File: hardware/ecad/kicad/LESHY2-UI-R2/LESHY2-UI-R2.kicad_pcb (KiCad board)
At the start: 6 copper layers, 80 x 150 mm, 432 parts, among them J1 Hirose FH34SRJ-50S-0.5SH(50), J10 Samtec FTSH-105-01-L-DV-K-P-TR, J11 GCT USB4105-GF-A, J12 GCT RFPC-SMA31-FN-175-A, J13 Hirose U.FL-R-SMT-1(80), J14 GCT RFPC-SMA31-FN-175-A, J15 Hirose U.FL-R-SMT-1(80), J16 GCT RFPC-SMA31-FN-175-A, J17 Hirose U.FL-R-SMT-1(80), J18 Hirose FX8C-80P-SV1(92), J2 Samtec FTSH-105-01-L-DV-K-P-TR, J3 GCT RFPC-SMA32-FN-175-A, J4 Hirose U.FL-R-SMT-1(80), J5 Hirose DM3AT-SF-PEJM5, J6 Samtec FTSH-105-01-L-DV-K-P-TR, J7 GCT RFPC-SMA32-FN-175-A, J8 Hirose U.FL-R-SMT-1(80), J9 GCT USB4105-GF-A, Q1 Diodes Incorporated DMN2056U-7, Q2 Diodes Incorporated 2N7002DW-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, Q3 Diodes Incorporated DMN2056U-7, Q4 Diodes Incorporated DMN2056U-7, Q5 Diodes Incorporated DMN2056U-7, Q6 Diodes Incorporated 2N7002DW-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, SW1 Alps Alpine SKRTLAE010, SW10 OMRON B3S-1100P, SW11 OMRON B3S-1100P, SW12 OMRON B3S-1100P, SW13 OMRON B3S-1100P, SW14 OMRON B3S-1100P, SW15 OMRON B3S-1100P, SW16 OMRON B3S-1100P, SW17 OMRON B3S-1100P, SW18 Alps Alpine SKRTLAE010, SW19 Alps Alpine SKRTLAE010, SW2 Alps Alpine SKRTLAE010, SW20 Alps Alpine SKRTLAE010, SW21 Alps Alpine SKRTLAE010, SW3 OMRON B3S-1100P, SW4 OMRON B3S-1100P, SW5 OMRON B3S-1100P, SW6 OMRON B3S-1100P, SW7 OMRON B3S-1100P, SW8 OMRON B3S-1100P, SW9 OMRON B3S-1100P, U1 ESP32-S3-WROOM-1U-N16R8, U10 Texas Instruments TPS22919DCKR, U11 SN74LVC1G07DCKR, U12 Texas Instruments TPD8E003DQDR, U13 TCA9539PWR, U14 ESP32-C5-WROOM-1U-N8R8, U15 Texas Instruments TPD4E05U06D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, U16 KYOCERA AVX CP0603Q5425ENTR, U17 74LVC2G14GV,125, U18 SN74LVC1G74DCUR, U19 74HC20PW,118, U2 Texas Instruments TPD4E05U06D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, U20 74LVC2G14GV,125, U21 Texas Instruments TPD2EUSB30A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, U22 onsemi FSUSB42MUX, U23 Vishay TSMP95000TT, U24 Vishay TSOP75238TR, U25 Texas Instruments TPS22919DCKR, U26 Nexperia 74LVC2G126DP,125, U27 SN74LVC1G08DCKR, U28 SC1512-A4, U29 Texas Instruments TPD4E05U06D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, U3 KYOCERA AVX CP0603Q5425ENTR, U30 Texas Instruments TPD2EUSB30A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, U31 onsemi FSUSB42MUX, U32 Analog Devices AD8314ARMZ-REEL, U33 Analog Devices AD8314ARMZ-REEL, U34 Analog Devices AD8314ARMZ-REEL, U35 Ebyte E01-ML01SP4, U36 TTM Technologies DC2337J5010A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, U37 Nexperia 74LVC126APW,118, U38 Nexperia 74LVC2G126DP,125, U39 Ebyte E01-ML01SP4, U4 Texas Instruments TPS2553DRVR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, U40 TTM Technologies DC2337J5010A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

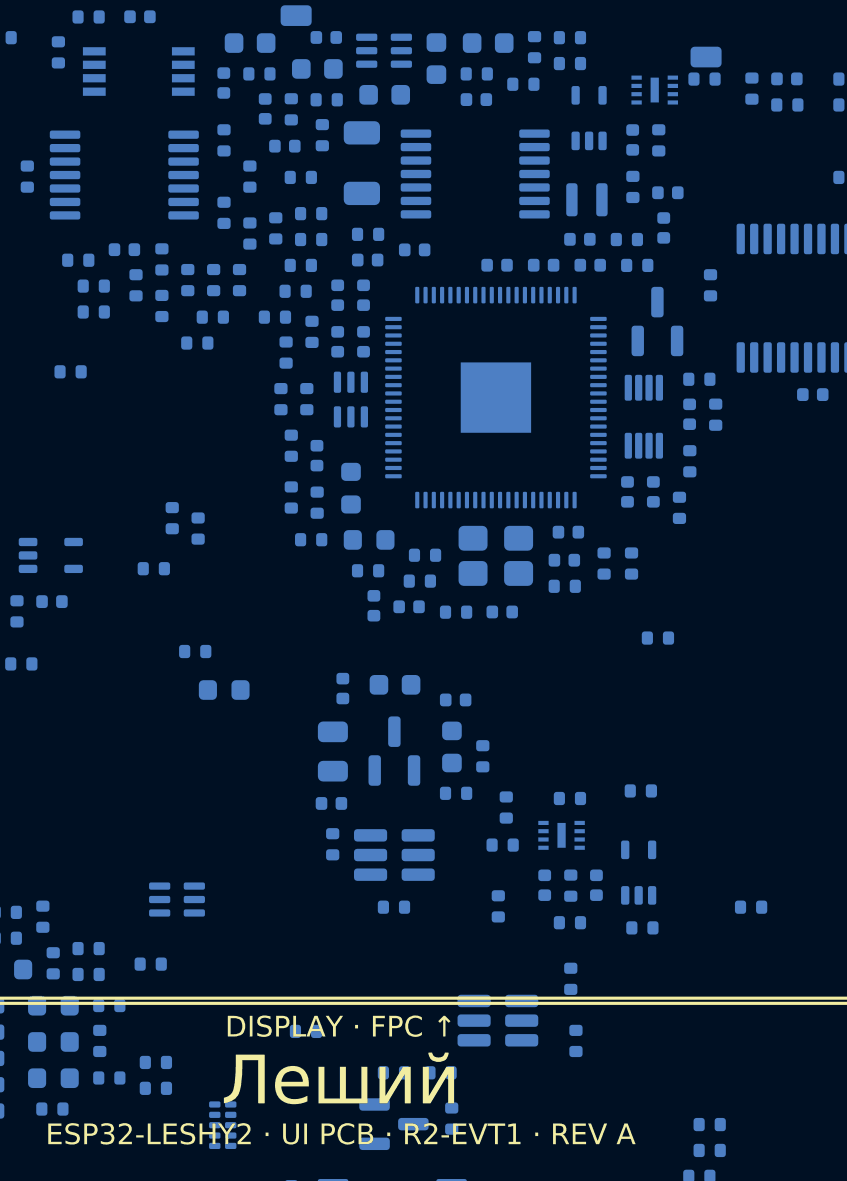
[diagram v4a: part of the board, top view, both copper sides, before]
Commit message: Audit critical placement by pad distance
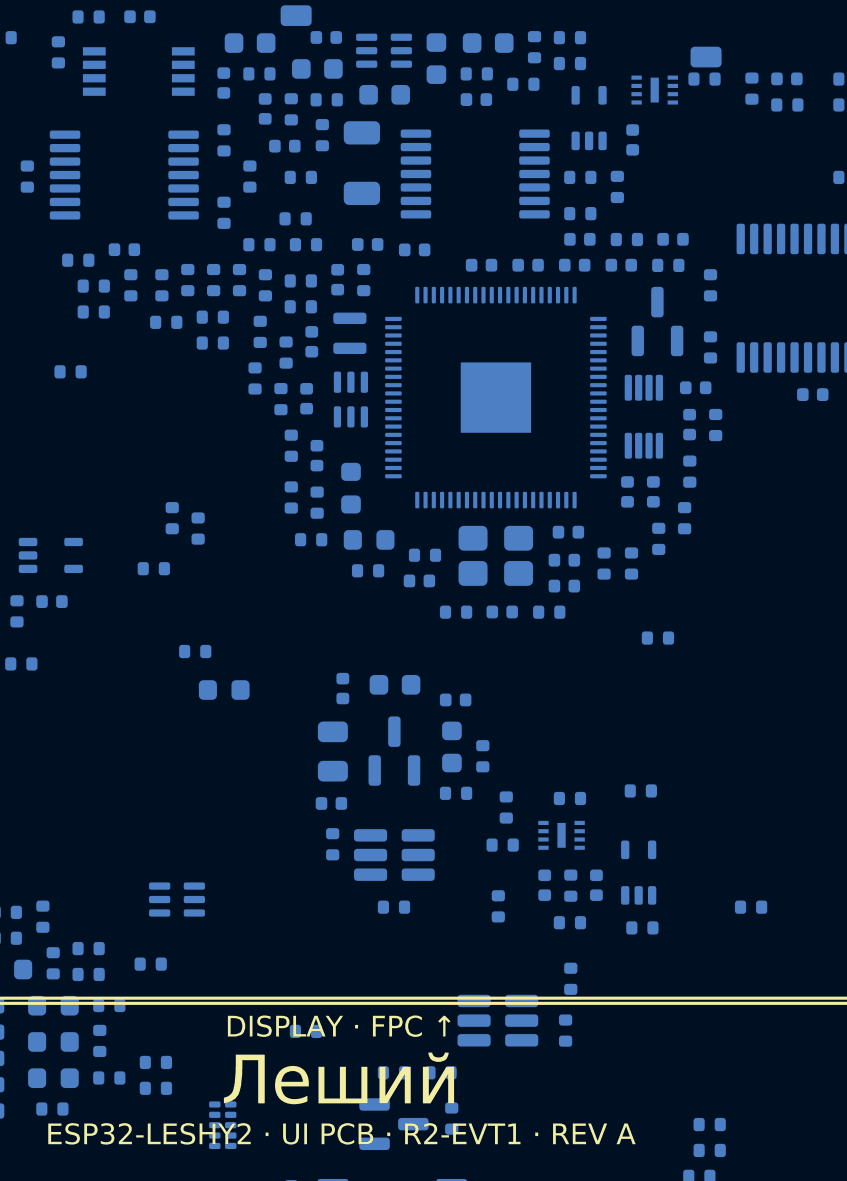
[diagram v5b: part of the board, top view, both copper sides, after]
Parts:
- moved R173 20.5 mm to (57.9, 72.6)
- moved C58 18.1 mm to (49.1, 68.6), turned to 0 degrees
- moved C56 17.6 mm to (41.3, 67.6)
- moved R192 16.5 mm to (50.1, 85.4), turned to 0 degrees
- moved C46 16.1 mm to (38.9, 77.8), turned to 90 degrees
- moved C52 15.7 mm to (43.8, 83.9)
- moved R145 14.8 mm to (41.1, 69.3), turned to 90 degrees
- moved C42 14.3 mm to (50.8, 82.9)
- moved C53 13.5 mm to (50.8, 84.1), turned to 0 degrees
- moved L1 13.1 mm to (40.4, 71.9), turned to 90 degrees
- moved C43 13.0 mm to (53.6, 68.6), turned to 0 degrees
- moved C41 12.6 mm to (53.9, 79.6), turned to 90 degrees
- moved C55 12.0 mm to (51.6, 67.4), turned to 0 degrees
- moved C50 11.9 mm to (39.9, 69.3), turned to 90 degrees
- moved R172 11.7 mm to (55.8, 68.6), turned to 0 degrees
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
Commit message: Start reviewed H6 manual copper
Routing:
- net /UI_30_HUB_RP_CORE_SERVICE/HUB_RP_VREG_LX_SW: track 0.00 -> 4.62 mm

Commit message: Route RP2354 crystal networks
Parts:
- moved R131 0.67 mm to (43.8, 82.0), turned to 90 degrees
- turned Y1 to 180 degrees
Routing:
- net /UI_30_HUB_RP_CORE_SERVICE/HUB_RP_XOUT_CRYSTAL: track 0.00 -> 9.49 mm
- net /UI_30_HUB_RP_CORE_SERVICE/HUB_RP_XIN: track 0.00 -> 7.61 mm
- net /UI_30_HUB_RP_CORE_SERVICE/HUB_RP_XOUT: track 0.00 -> 4.46 mm
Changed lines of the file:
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@@
 	(footprint "Crystal:Crystal_SMD_Abracon_ABM8G-4Pin_3.2x2.5mm"
 		(layer "B.Cu")
-		(at 47.495 82.645)
+		(at 47.495 82.645 180)
 		(descr "Abracon ABM8G, Miniature Ceramic Crystal, 3.2x2.5mm package, SMD, http://www.abracon.com/Resonators/ABM8G.pdf")
 		(property "Reference" "Y1"
-			(at 0 2.45 180)
+			(at 0 2.45 0)
 			(layer "B.SilkS")
 			(hide yes)
@@
 		)
 		(property "Value" "Abracon ABM8-272-T3"
-			(at 0 -2.45 180)
+			(at 0 -2.45 0)
 			(layer "B.Fab")
 			(hide yes)
@@
 		)
 		(property "Datasheet" ""
-			(at 0 0 180)
+			(at 0 0 0)
 			(layer "B.Fab")
 			(hide yes)
@@
 		)
 		(property "Description" "abracon_abm8_272_t3"
-			(at 0 0 180)
+			(at 0 0 0)
 			(layer "B.Fab")
 			(hide yes)
@@
 		)
 		(property "KiLib_Generator" "crystal_resonator_oscillator"
-			(at 0 0 180)
+			(at 0 0 0)
 			(layer "B.SilkS")
 			(hide yes)
@@
 		)
 		(property "Leshy2Instance" "hub_rp_clock"
-			(at 0 0 180)
+			(at 0 0 0)
 			(layer "B.SilkS")
 			(hide yes)
@@
 		(duplicate_pad_numbers_are_jumpers no)
 		(fp_line
-			(start -2.06 -1.71)
-			(end 2.06 -1.71)
+			(start -2.06 1.71)
+			(end -2.06 -1.71)
 			(stroke
 				(width 0.12)
@@
 		)
 		(fp_line
-			(start -2.06 1.71)
-			(end -2.06 -1.71)
+			(start -2.06 -1.71)
+			(end 2.06 -1.71)
 			(stroke
 				(width 0.12)
@@
 		)
 		(fp_text user "${REFERENCE}"
-			(at 0 0 180)
+			(at 0 0 0)
 			(layer "B.Fab")
 			(effects
@@
 		)
 		(pad "1" smd roundrect
-			(at -1.1 -0.85)
+			(at -1.1 -0.85 180)
 			(size 1.4 1.2)
 			(layers "B.Cu" "B.Mask" "B.Paste")
@@
 		)
 		(pad "2" smd roundrect
-			(at 1.1 -0.85)
+			(at 1.1 -0.85 180)
 			(size 1.4 1.2)
 			(layers "B.Cu" "B.Mask" "B.Paste")
@@
 		)
 		(pad "3" smd roundrect
-			(at 1.1 0.85)
+			(at 1.1 0.85 180)
 			(size 1.4 1.2)
 			(layers "B.Cu" "B.Mask" "B.Paste")
@@
 		)
 		(pad "4" smd roundrect
-			(at -1.1 0.85)
+			(at -1.1 0.85 180)
 			(size 1.4 1.2)
 			(layers "B.Cu" "B.Mask" "B.Paste")
@@
 	(footprint "Resistor_SMD:R_0402_1005Metric"
 		(layer "B.Cu")
-		(at 44.075 82.615 180)
+		(at 43.8 82 90)
 		(descr "Resistor SMD 0402 (1005 Metric), square (rectangular) end terminal, IPC-7351 nominal, (Body size source: IPC-SM-782 page 72, https://www.pcb-3d.com/wordpress/wp-content/uploads/ipc-sm-782a_amendment_1_and_2.pdf)")
 		(tags "resistor")
 		(property "Reference" "R131"
-			(at 0 1.17 0)
+			(at 0 1.17 270)
 			(layer "B.SilkS")
 			(hide yes)
@@
 		)
 		(property "Value" "Yageo RC0402FR-071KL"
-			(at 0 -1.17 0)
+			(at 0 -1.17 270)
 			(layer "B.Fab")
 			(hide yes)
@@
 		)
 		(property "Datasheet" ""
-			(at 0 0 0)
+			(at 0 0 270)
 			(layer "B.Fab")
 			(hide yes)
@@
 		)
 		(property "Description" "yageo_rc0402fr_071kl"
-			(at 0 0 0)
+			(at 0 0 270)
 			(layer "B.Fab")
 			(hide yes)
@@
 		)
 		(property "KiLib_Generator" "SMD_2terminal_chip_molded"
-			(at 0 0 0)
+			(at 0 0 270)
 			(layer "B.SilkS")
 			(hide yes)
@@
 		)
 		(property "Leshy2Instance" "hub_rp_clock_series"
-			(at 0 0 0)
+			(at 0 0 270)
 			(layer "B.SilkS")
 			(hide yes)
@@
 		(duplicate_pad_numbers_are_jumpers no)
 		(fp_line
-			(start -0.153641 0.38)
-			(end 0.153641 0.38)
+			(start -0.153641 -0.38)
+			(end 0.153641 -0.38)
 			(stroke
 				(width 0.12)
@@
 		)
 		(fp_line
-			(start -0.153641 -0.38)
-			(end 0.153641 -0.38)
+			(start -0.153641 0.38)
+			(end 0.153641 0.38)
 			(stroke
 				(width 0.12)
@@
 		)
 		(fp_text user "${REFERENCE}"
-			(at 0 0 0)
+			(at 0 0 270)
 			(layer "B.Fab")
 			(effects
@@
 		)
 		(pad "1" smd roundrect
-			(at -0.51 0 180)
+			(at -0.51 0 90)
 			(size 0.54 0.64)
 			(layers "B.Cu" "B.Mask" "B.Paste")
@@
 		)
 		(pad "2" smd roundrect
-			(at 0.51 0 180)
+			(at 0.51 0 90)
 			(size 0.54 0.64)
 			(layers "B.Cu" "B.Mask" "B.Paste")
@@
 	)
 	(segment
+		(start 49.55 80.7)
+		(end 50.52 81.5)
+		(width 0.15)
+		(layer "B.Cu")
+		(net "/UI_30_HUB_RP_CORE_SERVICE/HUB_RP_XIN")
+	)
+	(segment
+		(start 47.7 80.7)
+		(end 49.55 80.7)
+		(width 0.15)
+		(layer "B.Cu")
+		(net "/UI_30_HUB_RP_CORE_SERVICE/HUB_RP_XIN")
+	)
+	(segment
+		(start 47.7 79.95)
+		(end 47.7 80.7)
+		(width 0.15)
+		(layer "B.Cu")
+		(net "/UI_30_HUB_RP_CORE_SERVICE/HUB_RP_XIN")
+	)
+	(segment
+		(start 49.55 80.7)
+		(end 49.55 83.5)
+		(width 0.15)
+		(layer "B.Cu")
+		(net "/UI_30_HUB_RP_CORE_SERVICE/HUB_RP_XIN")
+	)
+	(segment
+		(start 49.55 83.5)
+		(end 48.595 83.495)
+		(width 0.15)
+		(layer "B.Cu")
+		(net "/UI_30_HUB_RP_CORE_SERVICE/HUB_RP_XIN")
+	)
+	(segment
+		(start 45 80.65)
+		(end 43.8 81.49)
+		(width 0.15)
+		(layer "B.Cu")
+		(net "/UI_30_HUB_RP_CORE_SERVICE/HUB_RP_XOUT")
+	)
+	(segment
+		(start 47.3 80.65)
+		(end 45 80.65)
+		(width 0.15)
+		(layer "B.Cu")
+		(net "/UI_30_HUB_RP_CORE_SERVICE/HUB_RP_XOUT")
+	)
+	(segment
+		(start 47.3 79.95)
+		(end 47.3 80.65)
+		(width 0.15)
+		(layer "B.Cu")
+		(net "/UI_30_HUB_RP_CORE_SERVICE/HUB_RP_XOUT")
+	)
+	(segment
 		(start 44.45 70.5)
 		(end 44.25 70.7)
@@
 		(net "/UI_30_HUB_RP_CORE_SERVICE/HUB_RP_VREG_LX_SW")
 	)
+	(segment
+		(start 46.395 81.795)
+		(end 45 82.4)
+		(width 0.15)
+		(layer "B.Cu")
+		(net "/UI_30_HUB_RP_CORE_SERVICE/HUB_RP_XOUT_CRYSTAL")
+	)
+	(segment
+		(start 47.325 84.5)
+		(end 47.325 85.355)
+		(width 0.15)
+		(layer "B.Cu")
+		(net "/UI_30_HUB_RP_CORE_SERVICE/HUB_RP_XOUT_CRYSTAL")
+	)
+	(segment
+		(start 45 82.4)
+		(end 45 84.5)
+		(width 0.15)
+		(layer "B.Cu")
+		(net "/UI_30_HUB_RP_CORE_SERVICE/HUB_RP_XOUT_CRYSTAL")
+	)
+	(segment
+		(start 45 84.5)
+		(end 47.325 84.5)
+		(width 0.15)
+		(layer "B.Cu")
+		(net "/UI_30_HUB_RP_CORE_SERVICE/HUB_RP_XOUT_CRYSTAL")
+	)
+	(segment
+		(start 43.8 82.51)
+		(end 46.395 81.795)
+		(width 0.15)
+		(layer "B.Cu")
+		(net "/UI_30_HUB_RP_CORE_SERVICE/HUB_RP_XOUT_CRYSTAL")
+	)
 	(embedded_fonts no)
